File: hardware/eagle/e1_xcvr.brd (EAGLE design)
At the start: 50 x 50 mm, 36 parts

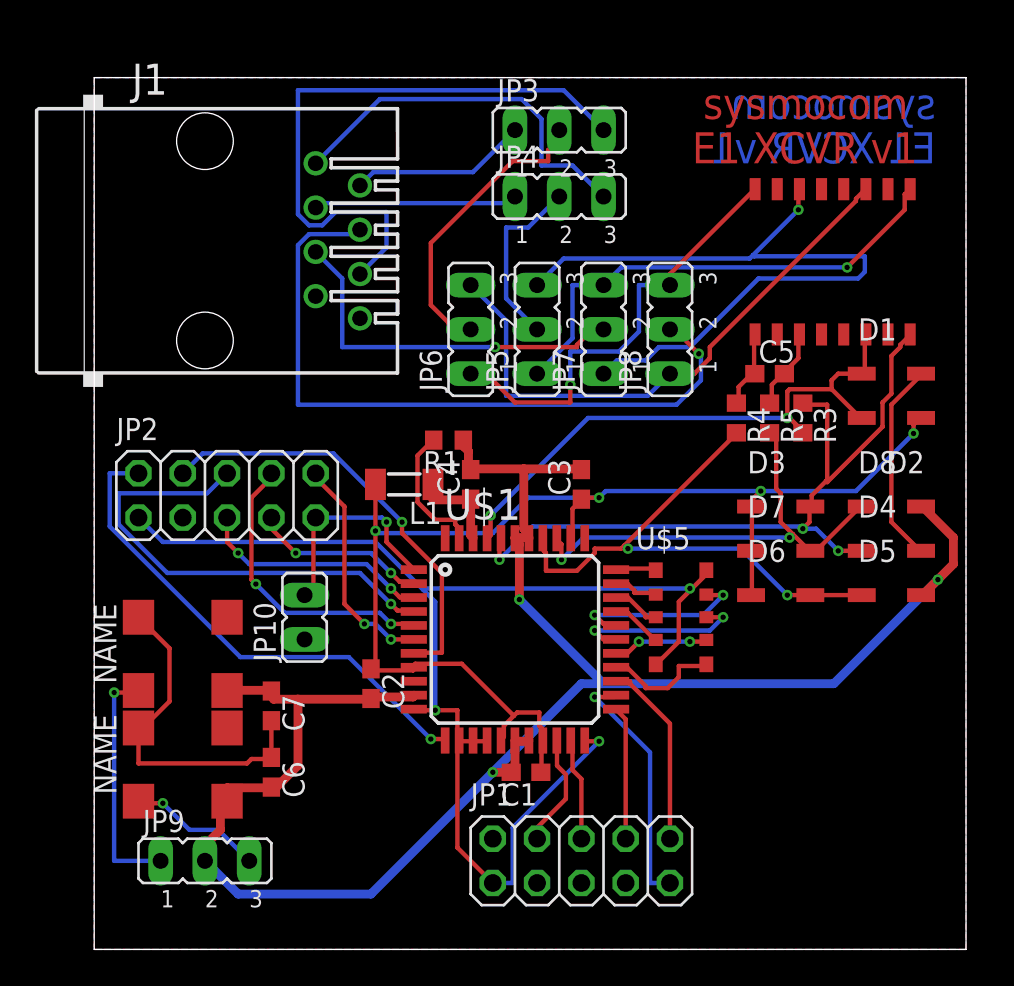
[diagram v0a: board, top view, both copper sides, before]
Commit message: Add LDO, remove jumpers, 3nd RJ45, ...
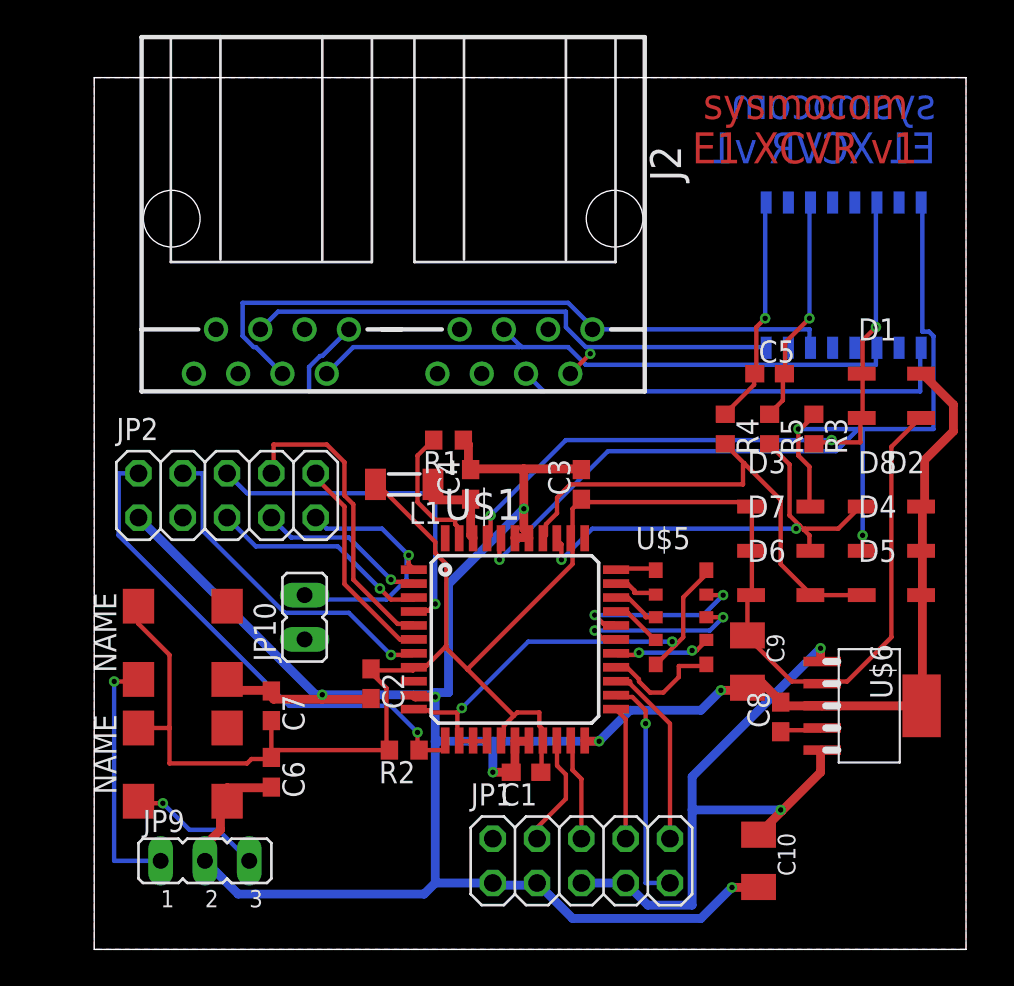
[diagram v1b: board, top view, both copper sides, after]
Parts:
- removed J1: (no value), con-amp:520251-4
- removed JP3, JP4: A/B, jumper:JP2
- removed JP5, JP6, JP7, JP8: TE/NT, jumper:JP2
- added C10: 68uF (NC), rcl:C1206K
- added C8: 1nF, rcl:C0603
- added C9: 68uF, rcl:C1206K
- added J2: (no value), con-amp:557560-1
- added R2: 10k, rcl:R0603
- added U$6: TPS736XX, laforge:SOT223-6
- U$3: value FOX_FXO-HC73 -> 2.048 Mhz
- U$4: value FOX_FXO-HC73 -> 1.544 MHz
- moved R3 0.90 mm to (41.3, 29.8)
- moved R4 0.90 mm to (36.2, 29.8)
- moved U$2 0.90 mm to (43.2, 38.7), flipped to the bottom, turned to 90 degrees
- moved R5 0.64 mm to (38.7, 29.8)
- moved U$4 0.63 mm to (2.54, 19.7)
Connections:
- removed net GNDT: D1.2, D4.2
- removed net N$24: C6.1, C7.2, U$3.P$4, U$4.P$4
- removed net N$33: JP5.3, JP7.1, U$2.P$11
- removed net N$42: JP6.1, JP8.3, U$2.P$9
- removed net R+: J1.4, JP8.2
- removed net R-: J1.5, JP7.2
- removed net T+A: J1.1, JP4.3
- removed net T+B: J1.3, JP4.1
- removed net T-A: J1.2, JP3.1
- removed net T-B: J1.6, JP3.3
- new net N$34: J2.1-4, J2.2-1, U$2.P$16
- new net VIN: C10.1, JP1.5, JP1.7, U$6.1, U$6.5
- net GND: now also C10.2, C8.2, C9.2, D1.2, D4.2, JP1.1, JP1.3, JP2.1, U$1.22, U$6.3, U$6.6
- net GNDIO: no longer JP1.1, JP2.1, U$1.22
- net N$17: now also R2.1
- net N$32: now also J2.1-2, J2.2-5, U$2.P$9; no longer JP5.1, JP7.3, U$2.P$16
- net N$36: now also J2.1-1, J2.2-4, U$2.P$11; no longer JP4.2, JP5.2
- net N$37: now also C8.1, U$6.4; no longer JP3.2, JP6.2
- net N$40: now also J2.1-5, J2.2-2; no longer JP6.3, JP8.1
- net VDD: now also C6.1, C7.2, C9.1, R2.2, U$3.P$4, U$4.P$4, U$6.2
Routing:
- net GND: track 109.0 -> 168.8 mm, vias 3 -> 7
- net GNDIO: track 74.5 -> 26.8 mm, vias 3 -> 2
- net N$34: track 0.00 -> 43.5 mm
- net N$33: track 42.7 -> 0.00 mm, vias 1 -> 0
- net VDD: track 71.9 -> 114.6 mm, vias 4 -> 0
- net R+: track 40.6 -> 0.00 mm, vias 1 -> 0
- net VIN: track 0.00 -> 37.1 mm, vias 0 -> 2
- net T-B: track 35.4 -> 0.00 mm
- net N$36: track 10.4 -> 39.4 mm
- net N$42: track 25.9 -> 0.00 mm, vias 1 -> 0
- net T+A: track 21.9 -> 0.00 mm
- net R-: track 21.6 -> 0.00 mm, vias 1 -> 0
- net N$24: track 20.0 -> 0.00 mm
- net N$28: track 43.2 -> 59.3 mm
- net N$37: track 17.4 -> 2.60 mm
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
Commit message: re-route the entire board to add test pads and additional components
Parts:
- added SJ1: (no value), jumper:SJ
- added TP1, TP2, TP3, TP4: TPPAD1-13, testpad:P1-13
- moved JP10 8.35 mm to (13.3, 10.8)
- moved C6 3.17 mm to (10.2, 6.99)
- moved JP9 2.01 mm to (5.71, 3.17)
- moved U$3 1.27 mm to (2.54, 11.4)
- moved U$4 1.27 mm to (2.54, 18.4)
- moved C2 0.64 mm to (16.5, 15.2)
- moved C3 0.64 mm to (27.9, 26.0)
- moved C4 0.64 mm to (21.6, 26.0)
- moved JP2 0.64 mm to (7.62, 25.4), turned to 180 degrees
- moved C7 0.63 mm to (10.2, 13.3)
- moved R2 0.63 mm to (18.4, 11.4)
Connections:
- net N$18 renamed MCLK
- net N$7 renamed TCLK
- removed net N$25: D5.1, D6.2, R4.2, U$1.37
- removed net N$26: JP1.10, U$1.25
- removed net N$27: D1.1, D2.2, R3.2, U$1.41, U$2.P$3
- removed net N$28: D3.2, D4.1, R3.1, U$1.40, U$2.P$1
- removed net N$30: D7.2, D8.1, R5.2, U$1.36
- new net N$19: JP1.8, U$1.24
- new net RRING: D3.2, D4.1, R3.1, TP2.TP, U$1.40, U$2.P$1
- new net RTIP: D1.1, D2.2, R3.2, TP1.TP, U$1.41, U$2.P$3
- new net TRING: D7.2, D8.1, R5.2, TP4.TP, U$1.36
- new net TTIP: D5.1, D6.2, R4.2, TP3.TP, U$1.37
- net GND: now also JP1.2; no longer JP1.1, JP1.3
- net N$20: now also JP1.10; no longer JP1.6
- net N$21: now also JP1.7; no longer JP1.8
- net N$22: now also U$1.25; no longer U$1.24
- net VDD: now also SJ1.2
- net VIN: now also JP1.1, SJ1.1; no longer JP1.5, JP1.7
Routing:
- net RTIP: track 0.00 -> 65.3 mm, vias 0 -> 2
- net N$28: track 59.3 -> 0.00 mm, vias 3 -> 0
- net RRING: track 0.00 -> 56.9 mm, vias 0 -> 4
- net N$27: track 39.9 -> 0.00 mm, vias 3 -> 0
- net TTIP: track 0.00 -> 33.7 mm, vias 0 -> 2
- net TRING: track 0.00 -> 29.8 mm, vias 0 -> 2
- net N$25: track 28.6 -> 0.00 mm
- net N$30: track 26.8 -> 0.00 mm, vias 2 -> 0
- net TCLK: track 15.1 -> 41.0 mm
- net N$34: track 43.5 -> 57.6 mm
- net N$26: track 10.8 -> 0.00 mm
- net N$15: track 9.84 -> 20.2 mm
- net N$19: track 0.00 -> 9.92 mm
- net N$16: track 12.7 -> 21.7 mm, vias 1 -> 0
- net N$2: track 12.3 -> 20.9 mm, vias 0 -> 1
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
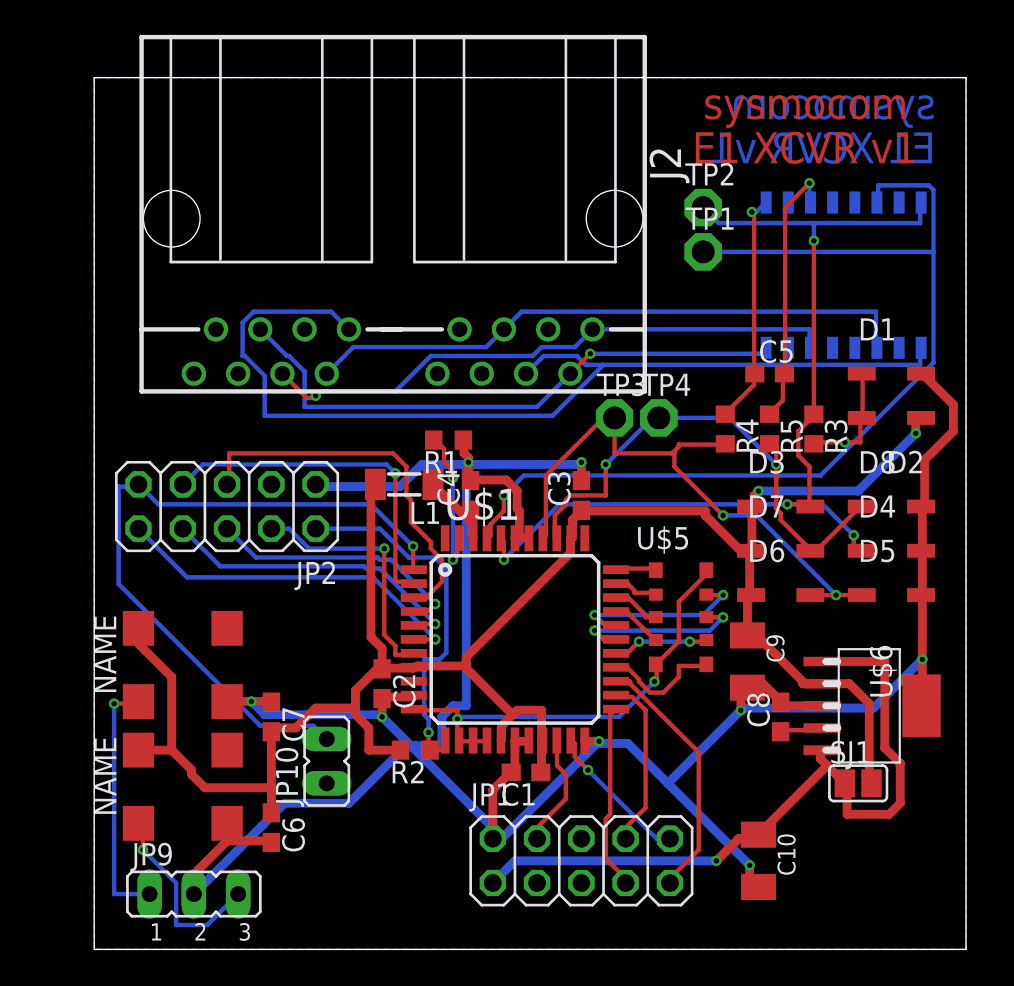
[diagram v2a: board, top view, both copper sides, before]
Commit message: re-route pcb with LEDs
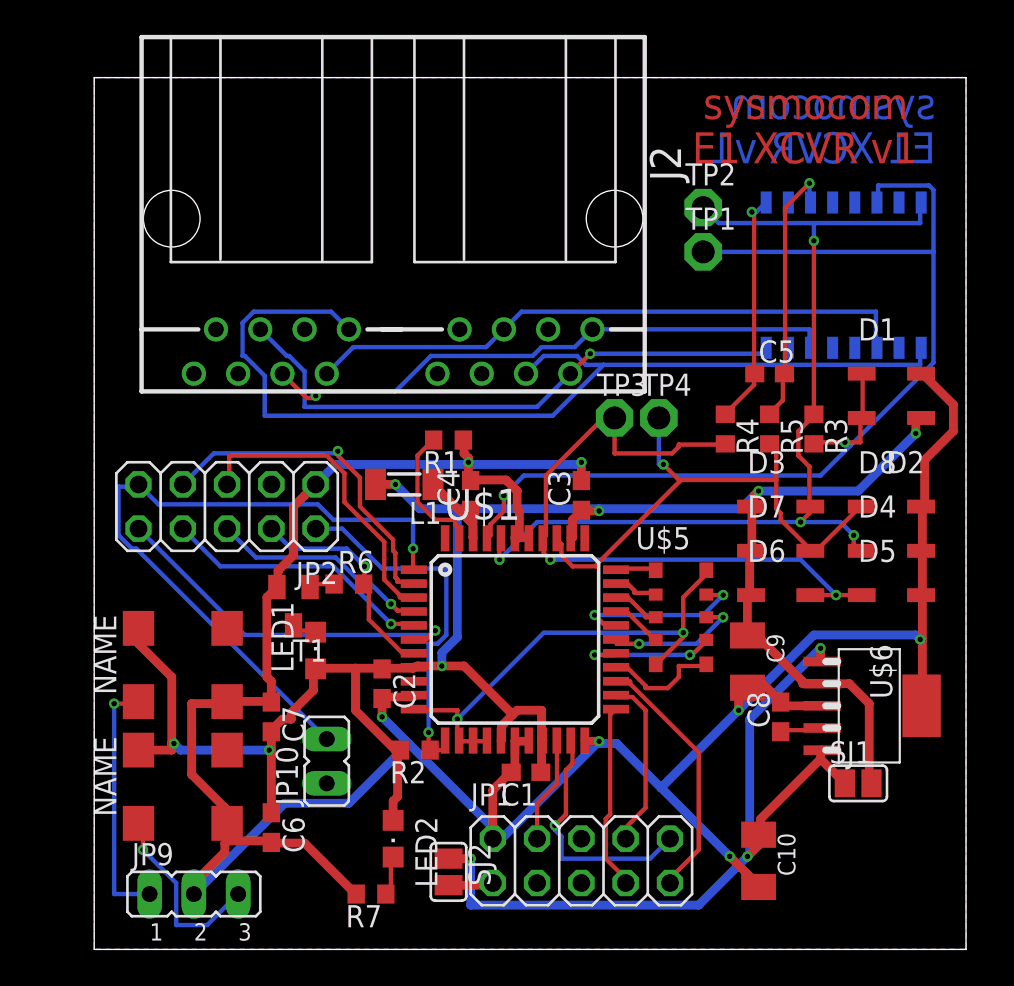
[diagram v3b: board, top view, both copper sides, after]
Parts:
- added LED1: RED, led:CHIPLED_0805
- added LED2: GREEN, led:CHIPLED_0805
- added R6: 10k, rcl:R0603
- added R7: 68, rcl:R0603
- added SJ2: (no value), jumper:SJ
- added T1: BC847C, transistor:SOT23-BEC
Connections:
- removed net N$5: JP2.4, U$1.7
- new net LOS: JP2.4, R6.2, U$1.7
- new net N$25: LED1.C, T1.C
- new net N$26: R6.1, T1.B
- new net N$30: LED2.C, R7.1
- new net N$7: JP1.1, SJ2.2
- net GND: now also R7.2, T1.E
- net VDD: now also LED1.A, LED2.A
- net VIN: now also SJ2.1; no longer JP1.1
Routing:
- net N$5: track 14.4 -> 0.00 mm, vias 1 -> 0
- net LOS: track 0.00 -> 12.8 mm, vias 0 -> 1
- net VDD: track 117.6 -> 124.4 mm, vias 2 -> 7
- net N$20: track 8.46 -> 14.1 mm
- net TTIP: track 33.7 -> 39.1 mm
- net N$16: track 21.7 -> 18.0 mm
- net VIN: track 41.8 -> 45.4 mm, vias 1 -> 3
- net GND: track 166.8 -> 170.2 mm, vias 8 -> 7
- net N$7: track 0.00 -> 2.67 mm
- net N$13: track 5.51 -> 8.04 mm
- net N$4: track 15.1 -> 12.7 mm
- net N$3: track 18.0 -> 15.6 mm
- net N$30: track 0.00 -> 2.32 mm
- net N$12: track 10.1 -> 7.99 mm
- net GNDIO: track 25.9 -> 27.6 mm
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
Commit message: re-route complete board, add PWR jumper, LED series resistor
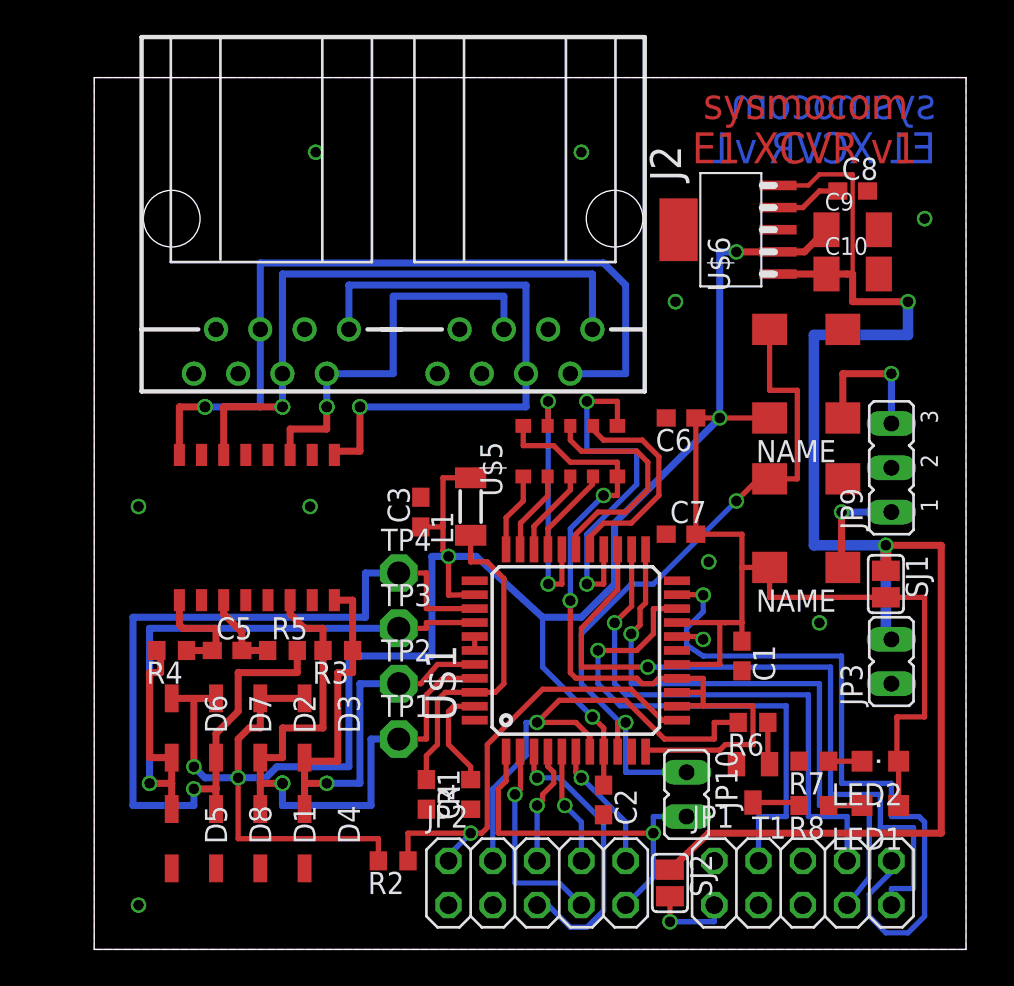
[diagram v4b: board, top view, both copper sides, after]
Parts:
- added JP3: PwrIn, jumper:JP1
- added R8: 68, rcl:R0603
- moved JP9 46.9 mm to (45.7, 27.6), turned to 90 degrees
- moved D1 45.0 mm to (9.53, 6.35), turned to 270 degrees
- moved D5 43.6 mm to (4.45, 6.35), turned to 270 degrees
- moved D8 43.2 mm to (6.99, 6.35), turned to 270 degrees
- moved U$3 40.9 mm to (38.7, 30.5), turned to 90 degrees
- moved D2 40.3 mm to (9.53, 12.7), turned to 270 degrees
- moved D4 37.5 mm to (12.1, 6.35), turned to 270 degrees
- moved U$2 36.7 mm to (9.53, 24.1), flipped to the top, turned to 270 degrees
- moved U$4 36.4 mm to (38.7, 21.9), turned to 90 degrees
- moved D6 35.7 mm to (4.45, 12.7), turned to 270 degrees
- moved C5 34.9 mm to (7.62, 17.1)
- moved R4 34.2 mm to (4.45, 17.1), turned to 180 degrees
- moved C10 34.1 mm to (43.5, 38.7), turned to 0 degrees
- moved D7 33.9 mm to (6.99, 12.7), turned to 270 degrees
- moved LED1 33.6 mm to (45.1, 8.26), turned to 90 degrees
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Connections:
- removed net GNDIO: U$1.11, U$1.13, U$1.14, U$1.15, U$5.10, U$5.5
- removed net N$25: LED1.C, T1.C
- new net N$18: R8.2, T1.C
- new net N$5: LED1.C, R8.1
- net GND: now also JP3.1, U$1.11, U$1.13, U$1.14, U$1.15, U$5.10, U$5.5
- net VIN: now also JP3.2
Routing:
- net GND: track 170.2 -> 47.1 mm, vias 7 -> 12
- net VDD: track 124.4 -> 172.0 mm, vias 7 -> 6
- net MCLK: track 0.00 -> 41.0 mm, vias 0 -> 2
- net VIN: track 45.4 -> 86.2 mm, vias 3 -> 2
- net RTIP: track 65.3 -> 37.3 mm
- net GNDIO: track 27.6 -> 0.00 mm, vias 2 -> 0
- net N$20: track 14.1 -> 41.0 mm
- net N$22: track 14.7 -> 41.5 mm, vias 0 -> 1
- net N$34: track 57.6 -> 33.4 mm, vias 0 -> 2
- net N$21: track 10.7 -> 34.8 mm, vias 0 -> 1
- net RRING: track 56.0 -> 32.0 mm, vias 4 -> 1
- net N$24: track 6.11 -> 30.1 mm, vias 0 -> 1
- net TRING: track 31.2 -> 53.7 mm
- net N$19: track 9.92 -> 31.2 mm, vias 0 -> 1
- net TCLK: track 40.3 -> 21.4 mm
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- added copper zone on layer 1, net GND
- added copper zone on layer 16, net GND
- removed copper zone on layer 1, net MCLK
- removed copper zone on layer 16, net VDD
